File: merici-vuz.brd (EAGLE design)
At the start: 160 x 100 mm, 53 parts, among them IC1 MEGA328-PB, IC2 MCP73831, IC3 LE33, Q1 3,6864 MHz, Q4 TSM2302CX, T1 IRF7306

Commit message: First prototype of PCB.
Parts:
- Q1: device crystal:HC49U70 -> crystal:HC49UP
- S-OFF, S-ON: value (none) -> P-DT2112C; device switch-omron:B3F-10XX -> switch-tact:DTSM-3
- TP1, TP2, TP3, TP4, TP5, TP6, TP7, TP8, TP9: value PTR1B2,54 -> PTR1B1,27; device testpad:B2,54 -> testpad:B1,27
- moved C11 111.9 mm to (44.5, 3.17), flipped to the bottom, turned to 270 degrees
- moved TP5 111.8 mm to (39.4, 6.67)
- moved TP3 108.4 mm to (45.7, 6.67)
- moved IC2 103.7 mm to (43.2, 3.17)
- moved R10 98.2 mm to (38.1, 14.9), flipped to the bottom, turned to 270 degrees
- moved R9 96.0 mm to (39.7, 5.71), flipped to the bottom
- moved TP1 95.7 mm to (38.7, 1.91)
- moved R8 95.6 mm to (38.7, 3.17), flipped to the bottom, turned to 90 degrees
- moved R11 95.3 mm to (39.7, 14.9), flipped to the bottom, turned to 90 degrees
- moved C1 94.4 mm to (27.0, 6.03)
- moved CON-OPTO 92.8 mm to (34.0, 2.22)
- moved TP4 90.5 mm to (25.4, 16.2)
- moved S-OFF 89.6 mm to (30.5, 15.2), turned to 180 degrees
- moved R4 87.0 mm to (32.4, 5.08)
- moved T1 87.0 mm to (39.7, 9.53), flipped to the bottom, turned to 270 degrees
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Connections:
- removed net RESET: CON-PROG.5
- net !RESET: now also CON-PROG.5
- net !SHUTDOWN: now also IC1.14; no longer IC1.24
- net !SHUTDOWN_INT: no longer S-OFF.2
- net BT-EN: now also IC1.27; no longer IC1.9
- net CR1: now also IC1.8; no longer IC1.7
- net CR2: now also IC1.7; no longer IC1.8
- net GND: now also S-OFF.2, S-ON.1; no longer S-OFF.3, S-OFF.4, S-ON.3, S-ON.4
- net LED-GR: now also IC1.24; no longer IC1.19
- net LED-RED: now also IC1.26; no longer IC1.27
- net LED-YEL: now also IC1.25; no longer IC1.28
- net START_BUTTON: no longer S-ON.1
- net VCC: no longer TP5.PP
- net VCC-BAT: now also TP5.PP
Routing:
- net VCC: track 0.00 -> 82.3 mm, vias 0 -> 4
- net BAT-POS-VCC: track 0.00 -> 55.9 mm, vias 0 -> 4
- net CHARGE-STAT: track 0.00 -> 42.0 mm, vias 0 -> 3
- net BAT-SENSE: track 0.00 -> 27.7 mm, vias 0 -> 1
- net OPTO-MEASURE: track 0.00 -> 23.4 mm, vias 0 -> 1
- net CR1: track 0.00 -> 22.9 mm
- net MISO: track 0.00 -> 22.1 mm, vias 0 -> 3
- net SCK: track 0.00 -> 19.1 mm, vias 0 -> 1
- net BT-EN: track 0.00 -> 18.5 mm
- net BT-STATE: track 0.00 -> 17.5 mm, vias 0 -> 1
- net MOSI: track 0.00 -> 17.5 mm, vias 0 -> 3
- net START_GATE: track 0.00 -> 17.5 mm, vias 0 -> 2
- net CR2: track 0.00 -> 16.1 mm
- net VCC-USB: track 0.00 -> 15.6 mm
- net BT-RXD: track 0.00 -> 14.3 mm
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- added copper zone on layer 1, net GND
- added copper zone on layer 16, net GND
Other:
- board size 160 x 100 mm -> 49.8 x 17.5 mm

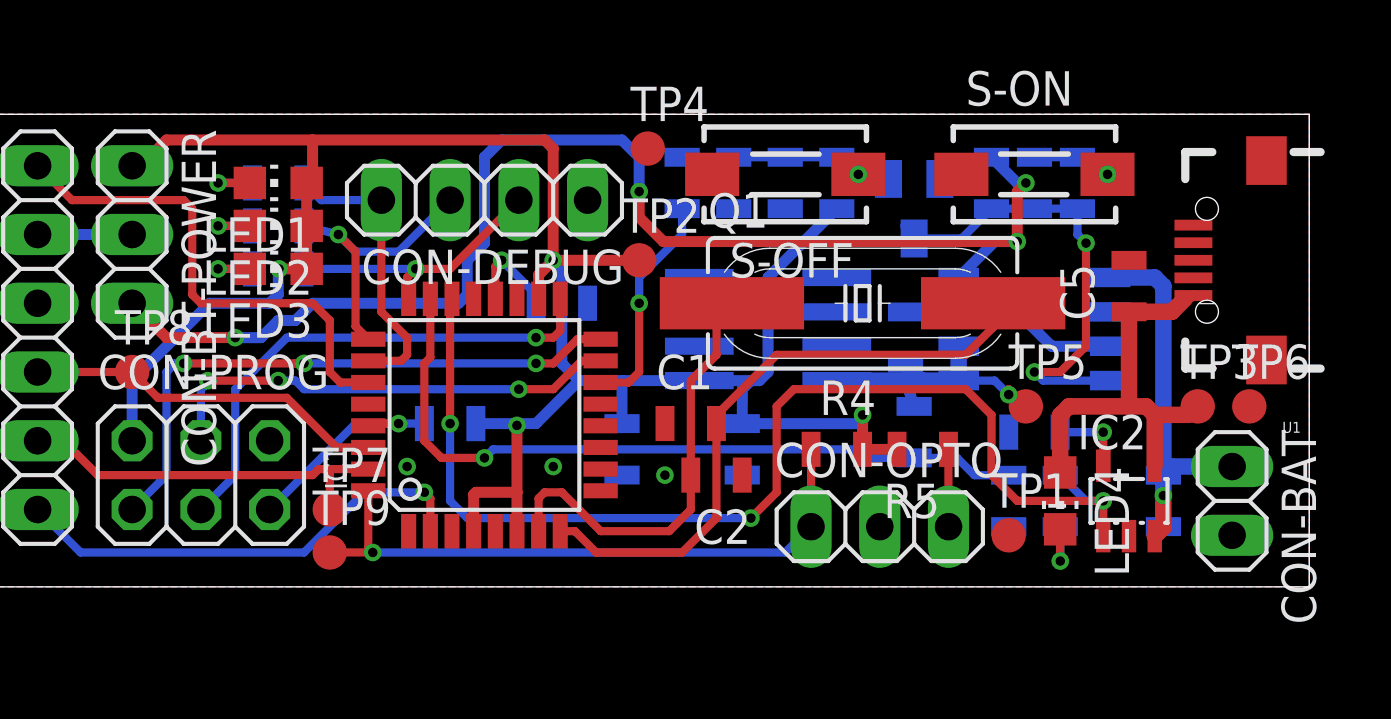
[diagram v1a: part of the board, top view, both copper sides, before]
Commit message: Board: pads, minor improvements.
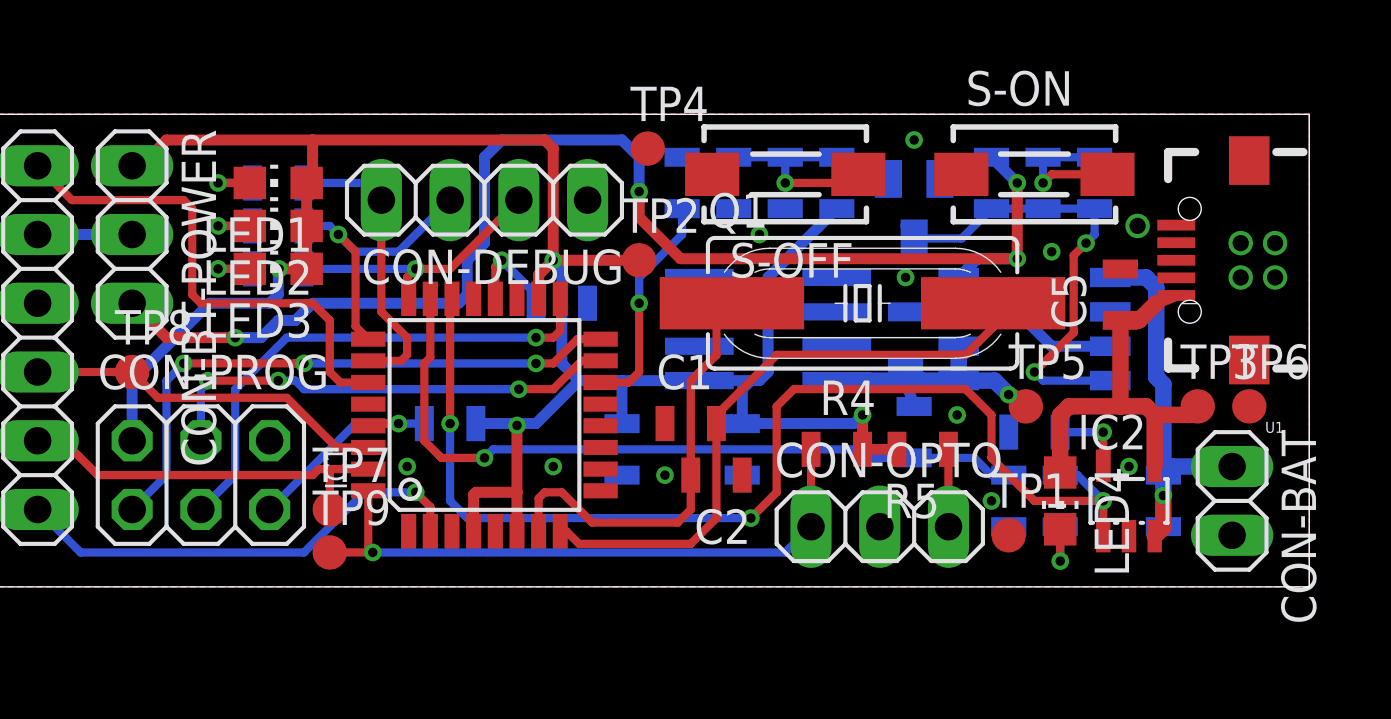
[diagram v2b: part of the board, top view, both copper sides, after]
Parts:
- moved C8 0.63 mm to (41.9, 14.9)
- moved U1 0.63 mm to (47.6, 12.1)
- moved C5 0.45 mm to (42.9, 10.8)
- moved R11 0.32 mm to (40.0, 14.9)
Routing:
- net !SHUTDOWN_INT: track 9.14 -> 12.2 mm
- net START_BUTTON: track 2.96 -> 5.37 mm
- net VCC-USB: track 15.6 -> 15.1 mm

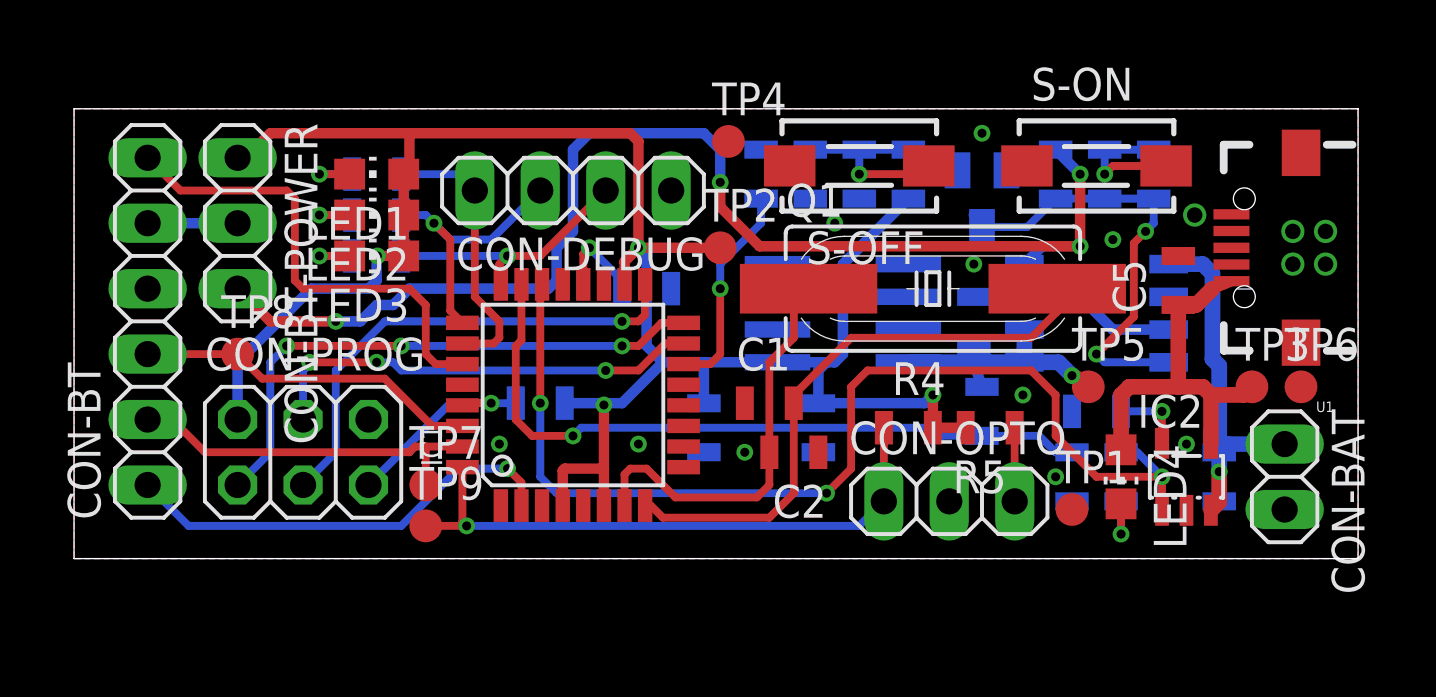
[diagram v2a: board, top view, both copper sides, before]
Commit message: Board: center pinheaders.
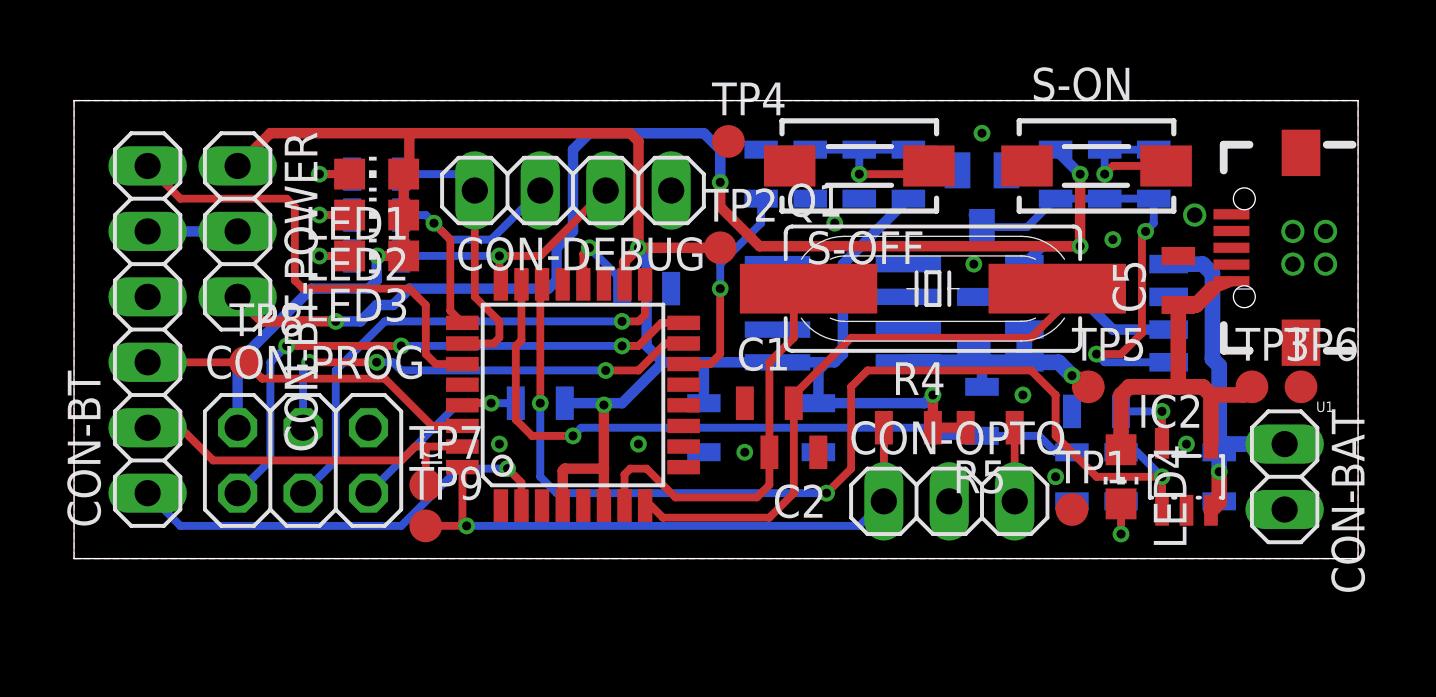
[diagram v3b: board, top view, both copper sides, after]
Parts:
- moved TP8 0.45 mm to (6.67, 7.62)
- moved CON-BT-POWER 0.32 mm to (6.35, 12.7)
- moved CON-PROG 0.32 mm to (8.89, 3.81)
- moved CON-BT 0.32 mm to (2.86, 8.89)
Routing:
- net START_GATE: track 17.6 -> 18.1 mm
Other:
- board size 49.8 x 17.5 mm -> 49.8 x 17.8 mm
